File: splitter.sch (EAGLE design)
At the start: 14 parts

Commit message: last minute changes
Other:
- moved on the sheet: C4, C6, C7, VREG
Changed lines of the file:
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@@
 <instance part="SUPPLY3" gate="G$1" x="106.68" y="114.3"/>
 <instance part="SUPPLY4" gate="G$1" x="101.6" y="71.12"/>
-<instance part="SUPPLY5" gate="G$1" x="33.02" y="27.94"/>
-<instance part="SUPPLY6" gate="G$1" x="88.9" y="27.94"/>
-<instance part="GND7" gate="1" x="45.72" y="-5.08"/>
-<instance part="C6" gate="G$1" x="83.82" y="17.78"/>
-<instance part="VREG" gate="G$1" x="60.96" y="20.32"/>
-<instance part="C7" gate="G$1" x="76.2" y="15.24" rot="R270"/>
-<instance part="C4" gate="G$1" x="38.1" y="17.78"/>
+<instance part="SUPPLY5" gate="G$1" x="48.26" y="43.18"/>
+<instance part="SUPPLY6" gate="G$1" x="104.14" y="43.18"/>
+<instance part="GND7" gate="1" x="60.96" y="10.16"/>
+<instance part="C6" gate="G$1" x="99.06" y="33.02"/>
+<instance part="VREG" gate="G$1" x="76.2" y="35.56"/>
+<instance part="C7" gate="G$1" x="91.44" y="30.48" rot="R270"/>
+<instance part="C4" gate="G$1" x="53.34" y="33.02"/>
 </instances>
 <busses>
@@
 <segment>
 <pinref part="SUPPLY6" gate="G$1" pin="3.3V"/>
-<wire x1="83.82" y1="25.4" x2="88.9" y2="25.4" width="0.1524" layer="91"/>
-<wire x1="88.9" y1="25.4" x2="88.9" y2="27.94" width="0.1524" layer="91"/>
+<wire x1="99.06" y1="40.64" x2="104.14" y2="40.64" width="0.1524" layer="91"/>
+<wire x1="104.14" y1="40.64" x2="104.14" y2="43.18" width="0.1524" layer="91"/>
 <pinref part="C6" gate="G$1" pin="+"/>
-<wire x1="83.82" y1="25.4" x2="83.82" y2="20.32" width="0.1524" layer="91"/>
-<wire x1="72.39" y1="25.4" x2="73.66" y2="25.4" width="0.1524" layer="91"/>
-<junction x="83.82" y="25.4"/>
+<wire x1="99.06" y1="40.64" x2="99.06" y2="35.56" width="0.1524" layer="91"/>
+<wire x1="87.63" y1="40.64" x2="88.9" y2="40.64" width="0.1524" layer="91"/>
+<junction x="99.06" y="40.64"/>
 <pinref part="VREG" gate="G$1" pin="VOUT"/>
-<wire x1="73.66" y1="25.4" x2="83.82" y2="25.4" width="0.1524" layer="91"/>
-<junction x="73.66" y="25.4"/>
+<wire x1="88.9" y1="40.64" x2="99.06" y2="40.64" width="0.1524" layer="91"/>
+<junction x="88.9" y="40.64"/>
 </segment>
 </net>
@@
 <segment>
 <pinref part="GND7" gate="1" pin="GND"/>
-<wire x1="45.72" y1="20.32" x2="45.72" y2="5.08" width="0.1524" layer="91"/>
-<wire x1="45.72" y1="5.08" x2="45.72" y2="-2.54" width="0.1524" layer="91"/>
-<wire x1="45.72" y1="5.08" x2="38.1" y2="5.08" width="0.1524" layer="91"/>
-<wire x1="38.1" y1="5.08" x2="38.1" y2="12.7" width="0.1524" layer="91"/>
-<junction x="45.72" y="5.08"/>
+<wire x1="60.96" y1="35.56" x2="60.96" y2="20.32" width="0.1524" layer="91"/>
+<wire x1="60.96" y1="20.32" x2="60.96" y2="12.7" width="0.1524" layer="91"/>
+<wire x1="60.96" y1="20.32" x2="53.34" y2="20.32" width="0.1524" layer="91"/>
+<wire x1="53.34" y1="20.32" x2="53.34" y2="27.94" width="0.1524" layer="91"/>
+<junction x="60.96" y="20.32"/>
 <pinref part="C6" gate="G$1" pin="-"/>
-<wire x1="45.72" y1="5.08" x2="76.2" y2="5.08" width="0.1524" layer="91"/>
-<wire x1="76.2" y1="5.08" x2="83.82" y2="5.08" width="0.1524" layer="91"/>
-<wire x1="83.82" y1="5.08" x2="83.82" y2="12.7" width="0.1524" layer="91"/>
+<wire x1="60.96" y1="20.32" x2="91.44" y2="20.32" width="0.1524" layer="91"/>
+<wire x1="91.44" y1="20.32" x2="99.06" y2="20.32" width="0.1524" layer="91"/>
+<wire x1="99.06" y1="20.32" x2="99.06" y2="27.94" width="0.1524" layer="91"/>
 <pinref part="VREG" gate="G$1" pin="GND"/>
-<wire x1="45.72" y1="20.32" x2="48.26" y2="20.32" width="0.1524" layer="91"/>
+<wire x1="60.96" y1="35.56" x2="63.5" y2="35.56" width="0.1524" layer="91"/>
 <pinref part="C7" gate="G$1" pin="1"/>
-<wire x1="76.2" y1="5.08" x2="76.2" y2="19.05" width="0.1524" layer="91"/>
-<junction x="76.2" y="5.08"/>
+<wire x1="91.44" y1="20.32" x2="91.44" y2="34.29" width="0.1524" layer="91"/>
+<junction x="91.44" y="20.32"/>
 <pinref part="C4" gate="G$1" pin="-"/>
 </segment>
@@
 <segment>
 <pinref part="SUPPLY5" gate="G$1" pin="VCC"/>
-<wire x1="38.1" y1="25.4" x2="33.02" y2="25.4" width="0.1524" layer="91"/>
-<wire x1="33.02" y1="25.4" x2="33.02" y2="27.94" width="0.1524" layer="91"/>
-<wire x1="38.1" y1="25.4" x2="38.1" y2="20.32" width="0.1524" layer="91"/>
-<wire x1="44.45" y1="25.4" x2="48.26" y2="25.4" width="0.1524" layer="91"/>
-<junction x="38.1" y="25.4"/>
+<wire x1="53.34" y1="40.64" x2="48.26" y2="40.64" width="0.1524" layer="91"/>
+<wire x1="48.26" y1="40.64" x2="48.26" y2="43.18" width="0.1524" layer="91"/>
+<wire x1="53.34" y1="40.64" x2="53.34" y2="35.56" width="0.1524" layer="91"/>
+<wire x1="59.69" y1="40.64" x2="63.5" y2="40.64" width="0.1524" layer="91"/>
+<junction x="53.34" y="40.64"/>
 <pinref part="VREG" gate="G$1" pin="VIN"/>
-<wire x1="48.26" y1="25.4" x2="43.18" y2="25.4" width="0.1524" layer="91"/>
-<junction x="48.26" y="25.4"/>
+<wire x1="63.5" y1="40.64" x2="58.42" y2="40.64" width="0.1524" layer="91"/>
+<junction x="63.5" y="40.64"/>
 <pinref part="VREG" gate="G$1" pin="ON/!OFF"/>
-<wire x1="43.18" y1="25.4" x2="38.1" y2="25.4" width="0.1524" layer="91"/>
-<wire x1="48.26" y1="15.24" x2="43.18" y2="15.24" width="0.1524" layer="91"/>
-<wire x1="43.18" y1="15.24" x2="43.18" y2="25.4" width="0.1524" layer="91"/>
-<junction x="43.18" y="25.4"/>
+<wire x1="58.42" y1="40.64" x2="53.34" y2="40.64" width="0.1524" layer="91"/>
+<wire x1="63.5" y1="30.48" x2="58.42" y2="30.48" width="0.1524" layer="91"/>
+<wire x1="58.42" y1="30.48" x2="58.42" y2="40.64" width="0.1524" layer="91"/>
+<junction x="58.42" y="40.64"/>
 <pinref part="C4" gate="G$1" pin="+"/>
 </segment>
@@
 <pinref part="VREG" gate="G$1" pin="BYPASS"/>
 <pinref part="C7" gate="G$1" pin="2"/>
-<wire x1="73.66" y1="20.32" x2="76.2" y2="20.32" width="0.1524" layer="91"/>
-<wire x1="76.2" y1="20.32" x2="76.2" y2="11.43" width="0.1524" layer="91"/>
+<wire x1="88.9" y1="35.56" x2="91.44" y2="35.56" width="0.1524" layer="91"/>
+<wire x1="91.44" y1="35.56" x2="91.44" y2="26.67" width="0.1524" layer="91"/>
 </segment>
 </net>

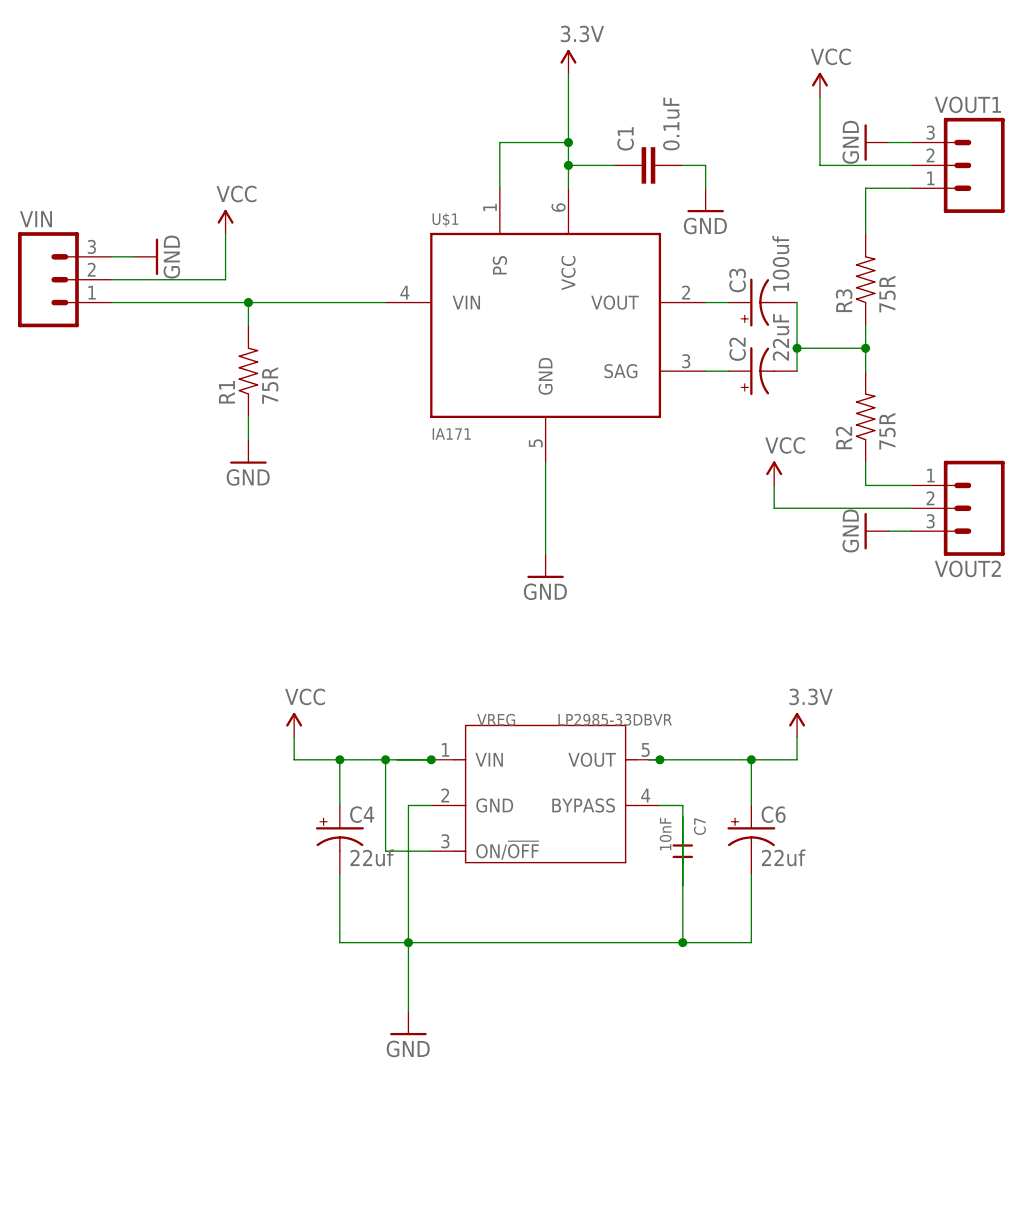
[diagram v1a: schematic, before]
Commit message: fixed cap values
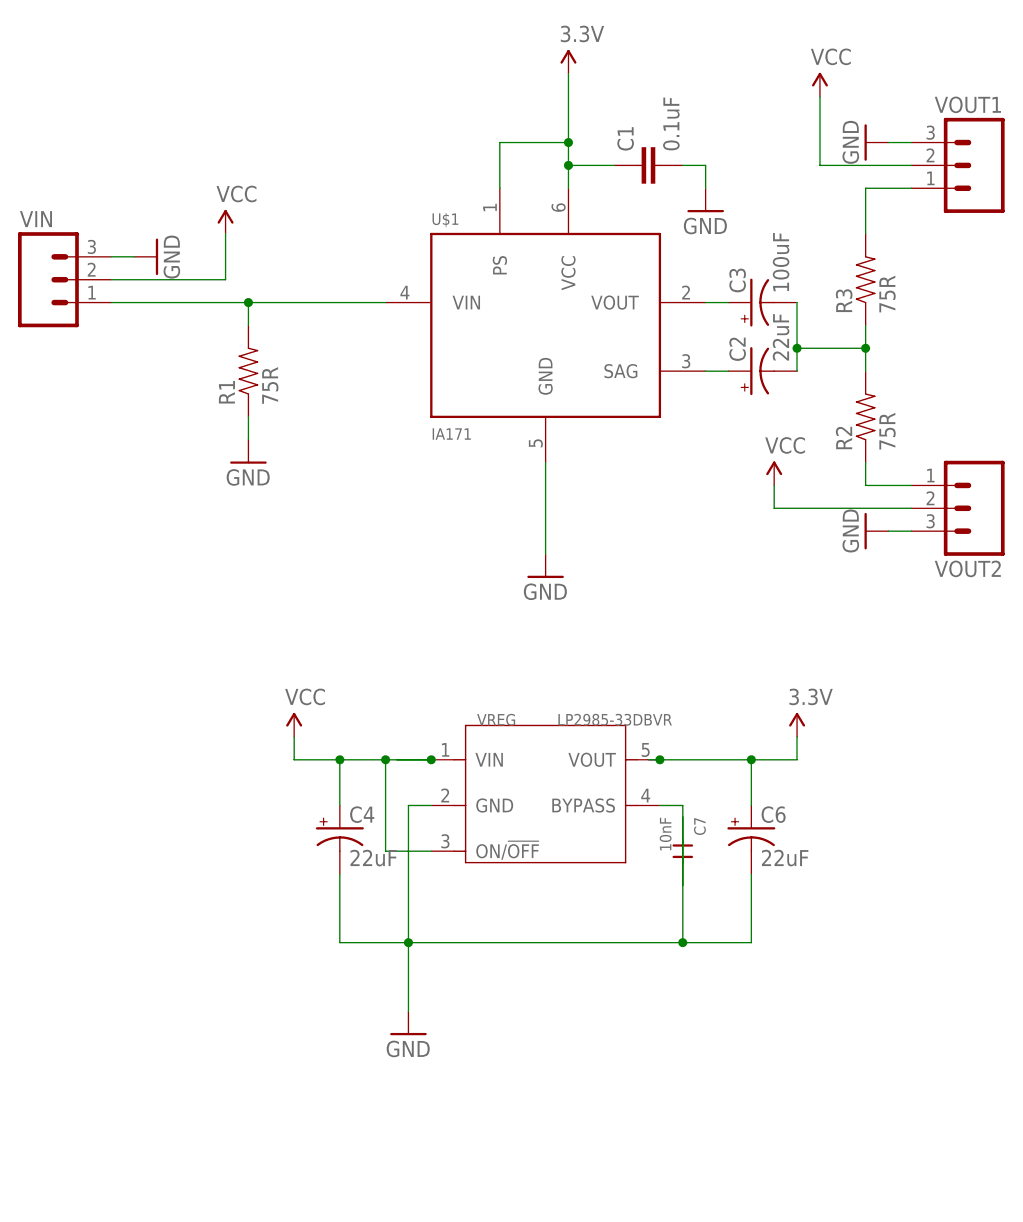
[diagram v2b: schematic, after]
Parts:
- C3: value 100uf -> 100uF
- C4, C6: value 22uf -> 22uF
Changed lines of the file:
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@@
 <part name="C2" library="SparkFun-Passives" deviceset="CAP_POL" device="1206" value="22uF"/>
 <part name="R1" library="SparkFun-Passives" deviceset="RESISTOR" device="0805-RES" value="75R"/>
-<part name="C3" library="SparkFun-Passives" deviceset="CAP_POL" device="3528" value="100uf"/>
+<part name="C3" library="SparkFun-Passives" deviceset="CAP_POL" device="3528" value="100uF"/>
 <part name="R2" library="SparkFun-Passives" deviceset="RESISTOR" device="0805-RES" value="75R"/>
 <part name="R3" library="SparkFun-Passives" deviceset="RESISTOR" device="0805-RES" value="75R"/>
@@
 <part name="SUPPLY6" library="SparkFun-Aesthetics" deviceset="3.3V" device=""/>
 <part name="GND7" library="SparkFun-Aesthetics" deviceset="GND" device=""/>
-<part name="C6" library="SparkFun-Passives" deviceset="CAP_POL" device="1206" value="22uf"/>
+<part name="C6" library="SparkFun-Passives" deviceset="CAP_POL" device="1206" value="22uF"/>
 <part name="VREG" library="Seeed-OPL-ic" deviceset="PMIC-LP2985-33DBVR(SOT23-5)" device="" value="LP2985-33DBVR"/>
 <part name="C7" library="Seeed-OPL-Capacitor" deviceset="CERAMIC-10NF-50V-5%-X7R(0805)" device="" value="10nF"/>
-<part name="C4" library="SparkFun-Passives" deviceset="CAP_POL" device="1206" value="22uf"/>
+<part name="C4" library="SparkFun-Passives" deviceset="CAP_POL" device="1206" value="22uF"/>
 </parts>
 <sheets>
